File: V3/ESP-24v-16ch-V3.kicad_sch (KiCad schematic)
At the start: 4 parts, among them J3 Conn_01x08, J4 Conn_01x08, J5 Conn_01x08, J6 Conn_01x08

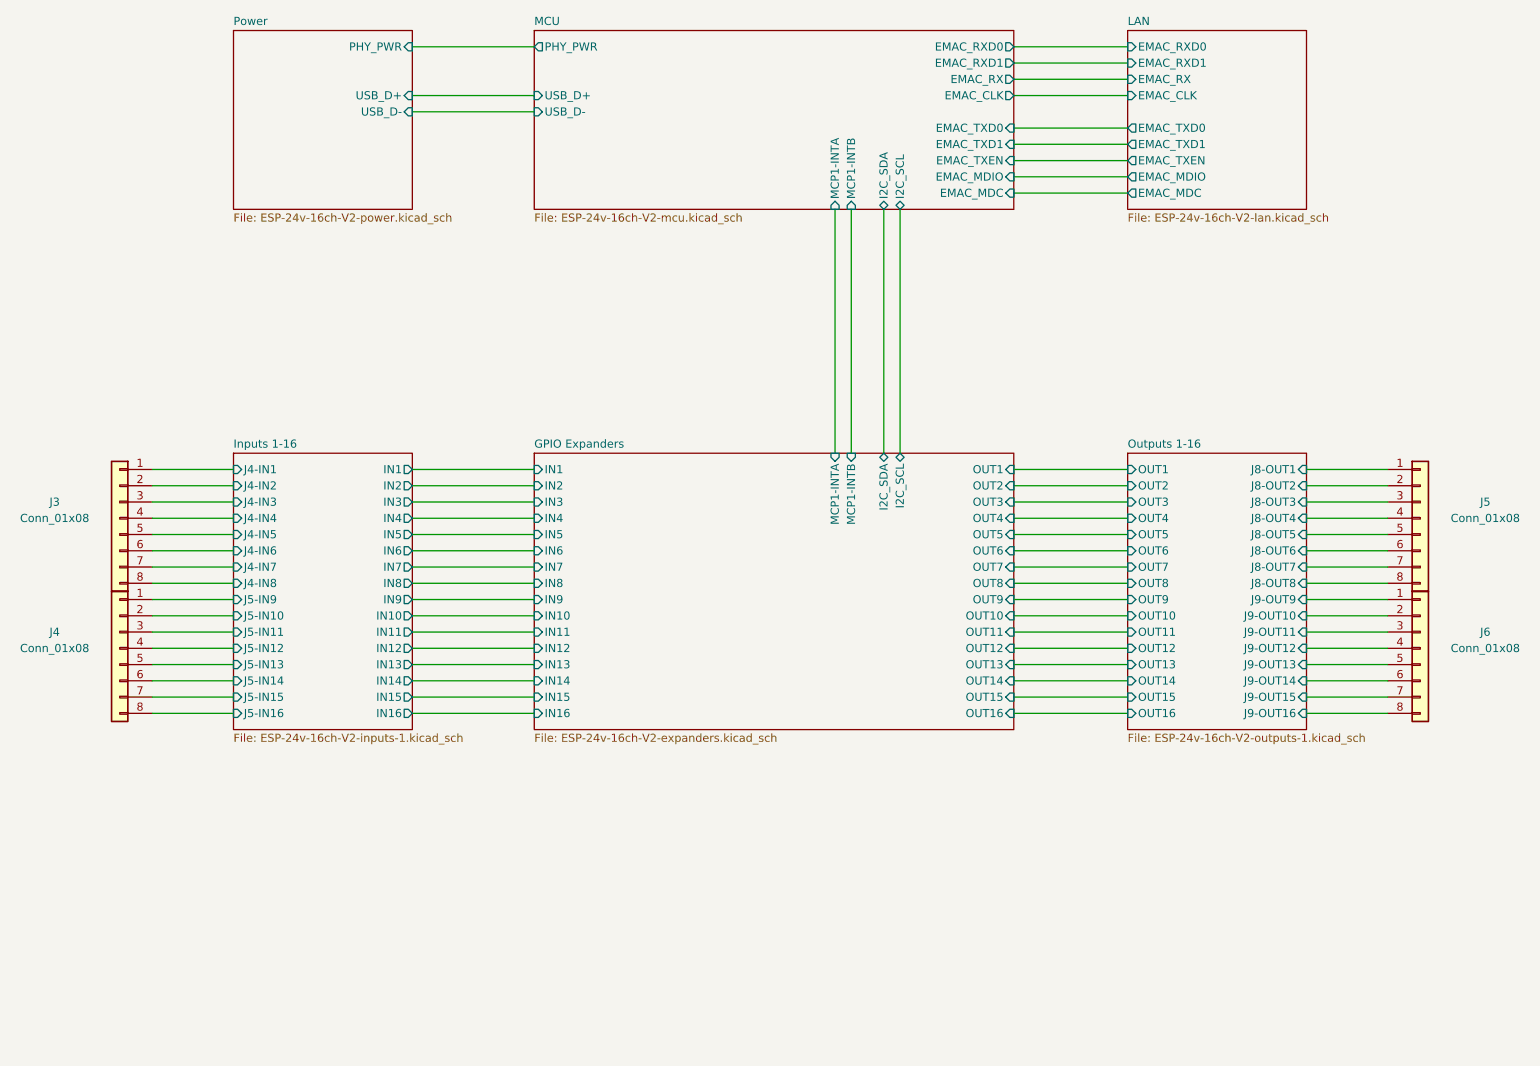
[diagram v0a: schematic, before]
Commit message: Connectors rotated 180deg
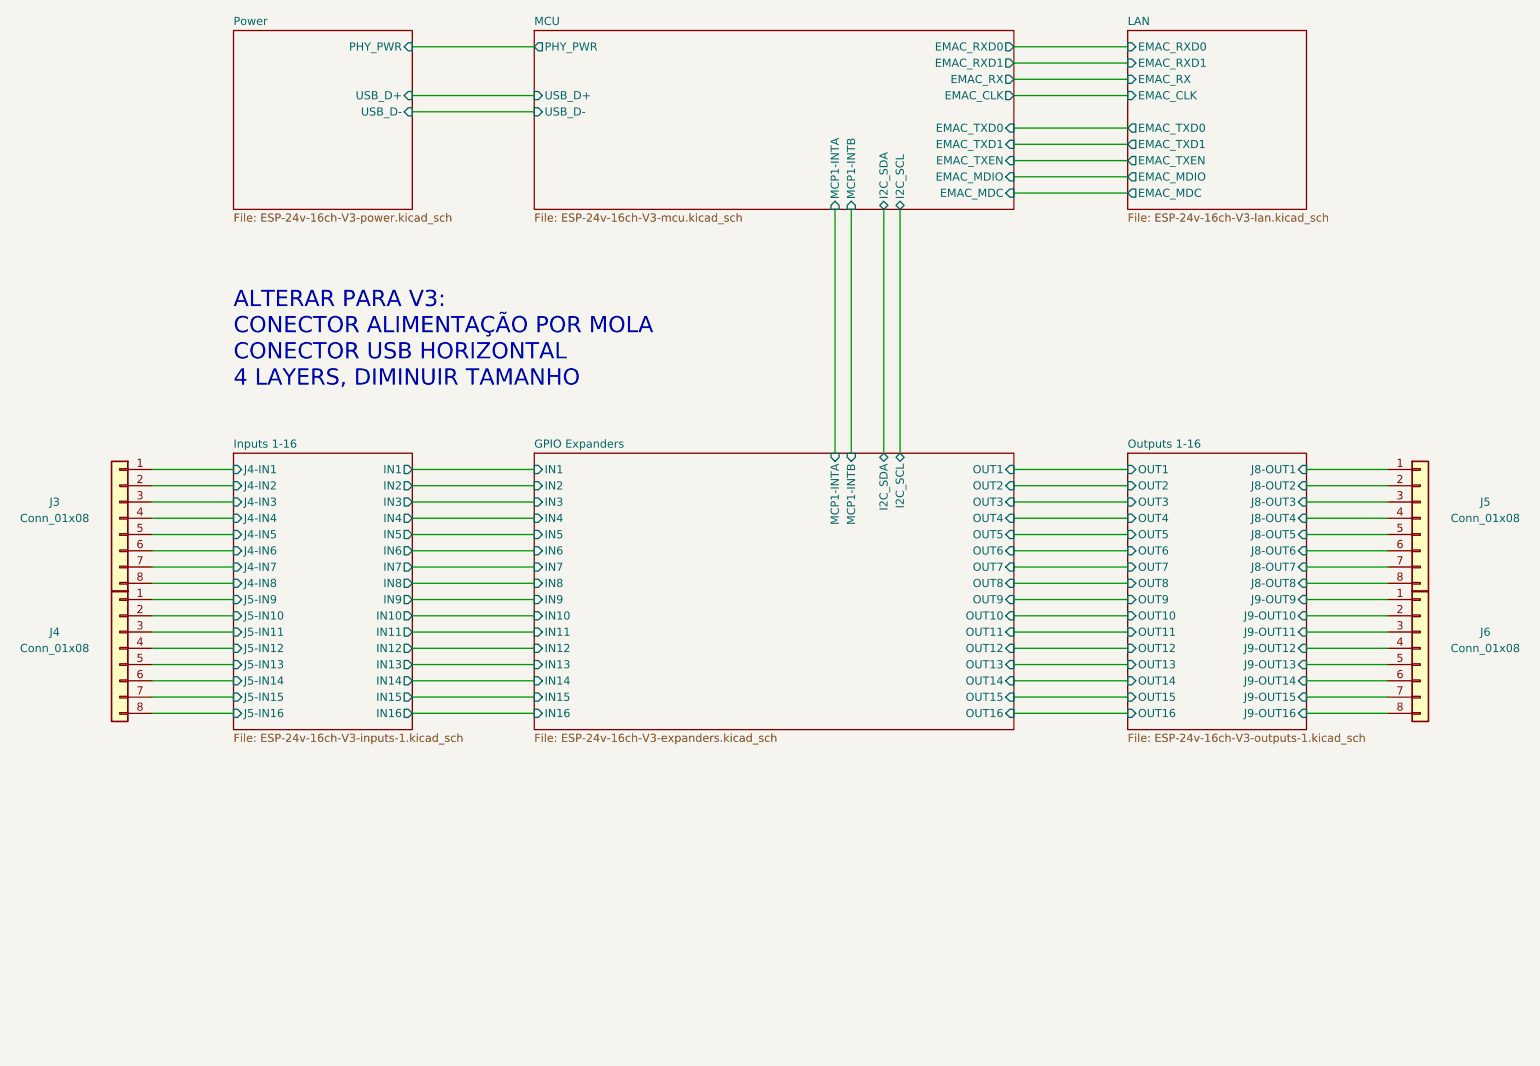
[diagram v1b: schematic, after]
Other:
- sheet GPIO Expanders: file ESP-24v-16ch-V2-expanders.kicad_sch -> ESP-24v-16ch-V3-expanders.kicad_sch
- sheet Inputs 1-16: file ESP-24v-16ch-V2-inputs-1.kicad_sch -> ESP-24v-16ch-V3-inputs-1.kicad_sch
- sheet LAN: file ESP-24v-16ch-V2-lan.kicad_sch -> ESP-24v-16ch-V3-lan.kicad_sch
- sheet MCU: file ESP-24v-16ch-V2-mcu.kicad_sch -> ESP-24v-16ch-V3-mcu.kicad_sch
- sheet Outputs 1-16: file ESP-24v-16ch-V2-outputs-1.kicad_sch -> ESP-24v-16ch-V3-outputs-1.kicad_sch
- sheet Power: file ESP-24v-16ch-V2-power.kicad_sch -> ESP-24v-16ch-V3-power.kicad_sch
- note added: "ALTERAR PARA V3: CONECTOR ALIMENTAÇÃO POR MOLA CONECTOR USB HORIZONTAL 4 LAYERS, DIMINUIR TAMANHO"
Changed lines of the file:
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@@
     (title "ESP 16x 24VDC Input 16x 24VDC Output Module")
     (date "2023-05-05")
-    (rev "V2")
+    (rev "V3")
   )
   (wire (pts (xy 91.44 133.35) (xy 110.49 133.35))
@@
   (wire (pts (xy 231.14 97.79) (xy 243.84 97.79))
     (stroke (width 0) (type default))
+  )
+  (text "ALTERAR PARA V3:\nCONECTOR ALIMENTAÇÃO POR MOLA\nCONECTOR USB HORIZONTAL\n4 LAYERS, DIMINUIR TAMANHO"
+    (at 63.5 82.55 0)
+    (effects (font (size 2.54 2.54)) (justify left bottom))
   )
   (symbol (lib_id "Connector_Generic:Conn_01x08") (at 248.92 123.19 0) (unit 1)
@@
     (pin "8")
     (instances
-      (project "ESP-24v-16ch-V2"
+      (project "ESP-24v-16ch-V3"
         (path "/2bc5a21a-1d79-419d-a592-6852cc07b00a"
           (reference "J6") (unit 1)
@@
     (pin "8")
     (instances
-      (project "ESP-24v-16ch-V2"
+      (project "ESP-24v-16ch-V3"
         (path "/2bc5a21a-1d79-419d-a592-6852cc07b00a"
           (reference "J5") (unit 1)
@@
     (pin "8")
     (instances
-      (project "ESP-24v-16ch-V2"
+      (project "ESP-24v-16ch-V3"
         (path "/2bc5a21a-1d79-419d-a592-6852cc07b00a"
           (reference "J4") (unit 1)
@@
     (pin "8")
     (instances
-      (project "ESP-24v-16ch-V2"
+      (project "ESP-24v-16ch-V3"
         (path "/2bc5a21a-1d79-419d-a592-6852cc07b00a"
           (reference "J3") (unit 1)
@@
       (effects (font (size 1.27 1.27)) (justify left bottom))
     )
-    (property "Sheetfile" "ESP-24v-16ch-V2-outputs-1.kicad_sch" (at 203.2 136.4746 0)
+    (property "Sheetfile" "ESP-24v-16ch-V3-outputs-1.kicad_sch" (at 203.2 136.4746 0)
       (effects (font (size 1.27 1.27)) (justify left top))
     )
@@
     )
     (instances
-      (project "ESP-24v-16ch-V2"
+      (project "ESP-24v-16ch-V3"
         (path "/2bc5a21a-1d79-419d-a592-6852cc07b00a" (page "8"))
       )
@@
       (effects (font (size 1.27 1.27)) (justify left bottom))
     )
-    (property "Sheetfile" "ESP-24v-16ch-V2-power.kicad_sch" (at 63.5 55.1946 0)
+    (property "Sheetfile" "ESP-24v-16ch-V3-power.kicad_sch" (at 63.5 55.1946 0)
       (effects (font (size 1.27 1.27)) (justify left top))
     )
@@
     )
     (instances
-      (project "ESP-24v-16ch-V2"
+      (project "ESP-24v-16ch-V3"
         (path "/2bc5a21a-1d79-419d-a592-6852cc07b00a" (page "2"))
       )
@@
       (effects (font (size 1.27 1.27)) (justify left bottom))
     )
-    (property "Sheetfile" "ESP-24v-16ch-V2-inputs-1.kicad_sch" (at 63.5 136.4746 0)
+    (property "Sheetfile" "ESP-24v-16ch-V3-inputs-1.kicad_sch" (at 63.5 136.4746 0)
       (effects (font (size 1.27 1.27)) (justify left top))
     )
@@
     )
     (instances
-      (project "ESP-24v-16ch-V2"
+      (project "ESP-24v-16ch-V3"
         (path "/2bc5a21a-1d79-419d-a592-6852cc07b00a" (page "6"))
       )
@@
       (effects (font (size 1.27 1.27)) (justify left bottom))
     )
-    (property "Sheetfile" "ESP-24v-16ch-V2-expanders.kicad_sch" (at 110.49 136.4746 0)
+    (property "Sheetfile" "ESP-24v-16ch-V3-expanders.kicad_sch" (at 110.49 136.4746 0)
       (effects (font (size 1.27 1.27)) (justify left top))
     )
@@
     )
     (instances
-      (project "ESP-24v-16ch-V2"
+      (project "ESP-24v-16ch-V3"
         (path "/2bc5a21a-1d79-419d-a592-6852cc07b00a" (page "5"))
       )
@@
       (effects (font (size 1.27 1.27)) (justify left bottom))
     )
-    (property "Sheetfile" "ESP-24v-16ch-V2-lan.kicad_sch" (at 203.2 55.1946 0)
+    (property "Sheetfile" "ESP-24v-16ch-V3-lan.kicad_sch" (at 203.2 55.1946 0)
       (effects (font (size 1.27 1.27)) (justify left top))
     )
@@
     )
     (instances
-      (project "ESP-24v-16ch-V2"
+      (project "ESP-24v-16ch-V3"
         (path "/2bc5a21a-1d79-419d-a592-6852cc07b00a" (page "4"))
       )
@@
       (effects (font (size 1.27 1.27)) (justify left bottom))
     )
-    (property "Sheetfile" "ESP-24v-16ch-V2-mcu.kicad_sch" (at 110.49 55.1946 0)
+    (property "Sheetfile" "ESP-24v-16ch-V3-mcu.kicad_sch" (at 110.49 55.1946 0)
       (effects (font (size 1.27 1.27)) (justify left top))
     )
@@
     )
     (instances
-      (project "ESP-24v-16ch-V2"
+      (project "ESP-24v-16ch-V3"
         (path "/2bc5a21a-1d79-419d-a592-6852cc07b00a" (page "3"))
       )

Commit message: Reviewing designs
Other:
- note added: "ALTERAR PARA V3: REVISAR TAMANHOS COMPONENTES TROCAR CONECTOR ALIMENTAÇÃO POR MOLA TROCAR CONECTOR USB POR HORIZONTAL 4 LAYERS, DIMINUIR TAMANHO RPACKS ONDE POSSÍVEL"
- note removed: "ALTERAR PARA V3: CONECTOR ALIMENTAÇÃO POR MOLA CONECTOR USB HORIZONTAL 4 LAYERS, DIMINUIR TAMANHO"
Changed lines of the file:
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@@
     (stroke (width 0) (type default))
   )
-  (text "ALTERAR PARA V3:\nCONECTOR ALIMENTAÇÃO POR MOLA\nCONECTOR USB HORIZONTAL\n4 LAYERS, DIMINUIR TAMANHO"
+  (text "ALTERAR PARA V3:\nREVISAR TAMANHOS COMPONENTES\nTROCAR CONECTOR ALIMENTAÇÃO POR MOLA\nTROCAR CONECTOR USB POR HORIZONTAL\n4 LAYERS, DIMINUIR TAMANHO\nRPACKS ONDE POSSÍVEL"
     (at 63.5 82.55 0)
     (effects (font (size 2.54 2.54)) (justify left bottom))

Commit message: Repository reorg and cleanup
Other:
- note added: "ALTERAR PARA V3: REVISAR TAMANHOS COMPONENTES TROCAR CONECTOR ALIMENTAÇÃO POR MOLA TROCAR CONECTOR USB POR HORIZONTAL 4 LAYERS, DIMINUIR TAMANHO RPACKS ONDE POSSÍVEL CHAVE RESET C520860 OU C520861 AVALIAR CUSTO"
- note removed: "ALTERAR PARA V3: REVISAR TAMANHOS COMPONENTES TROCAR CONECTOR ALIMENTAÇÃO POR MOLA TROCAR CONECTOR USB POR HORIZONTAL 4 LAYERS, DIMINUIR TAMANHO RPACKS ONDE POSSÍVEL"
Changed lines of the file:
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@@
     (stroke (width 0) (type default))
   )
-  (text "ALTERAR PARA V3:\nREVISAR TAMANHOS COMPONENTES\nTROCAR CONECTOR ALIMENTAÇÃO POR MOLA\nTROCAR CONECTOR USB POR HORIZONTAL\n4 LAYERS, DIMINUIR TAMANHO\nRPACKS ONDE POSSÍVEL"
-    (at 63.5 82.55 0)
+  (text "ALTERAR PARA V3:\nREVISAR TAMANHOS COMPONENTES\nTROCAR CONECTOR ALIMENTAÇÃO POR MOLA\nTROCAR CONECTOR USB POR HORIZONTAL\n4 LAYERS, DIMINUIR TAMANHO\nRPACKS ONDE POSSÍVEL\nCHAVE RESET C520860 OU C520861 AVALIAR CUSTO"
+    (at 31.75 185.42 0)
     (effects (font (size 2.54 2.54)) (justify left bottom))
   )
